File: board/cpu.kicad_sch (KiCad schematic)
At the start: 6 parts, among them U4 MC68000P

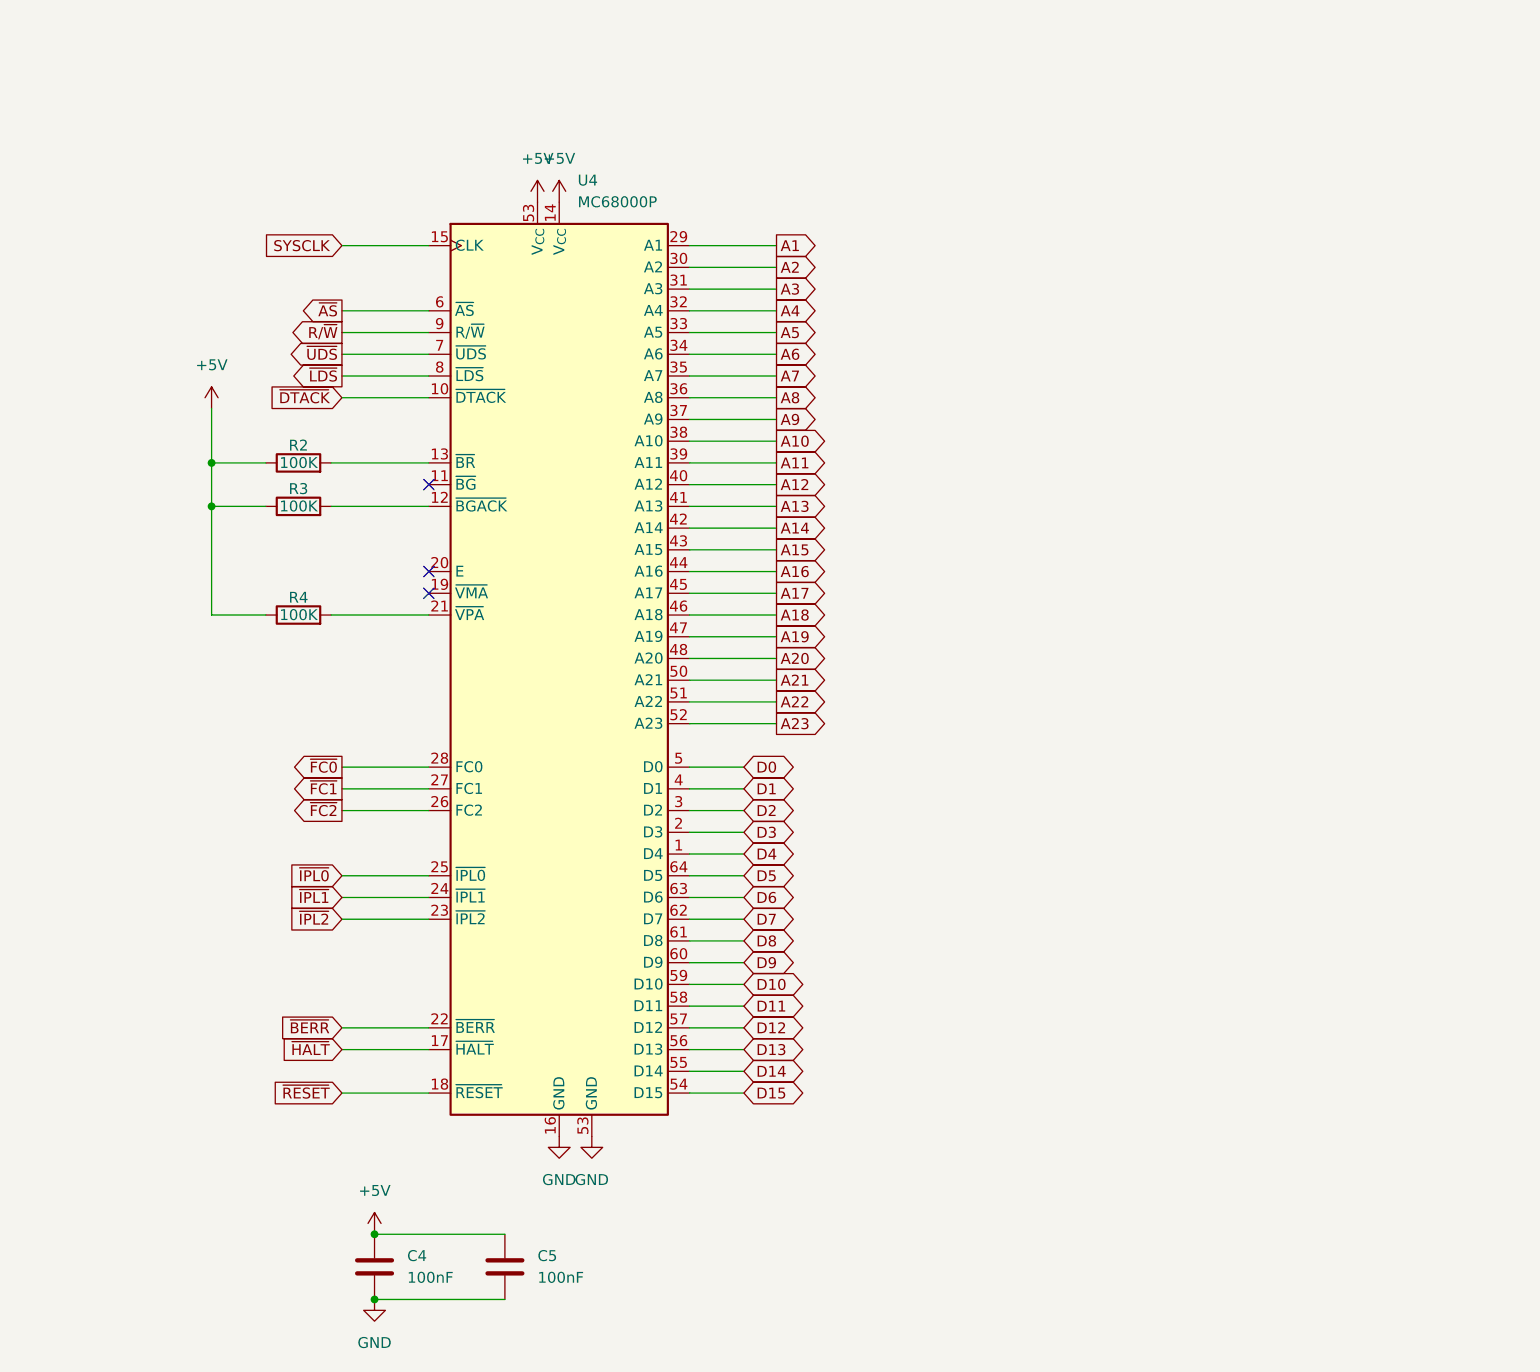
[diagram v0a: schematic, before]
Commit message: fill out most functionality - passes ERC
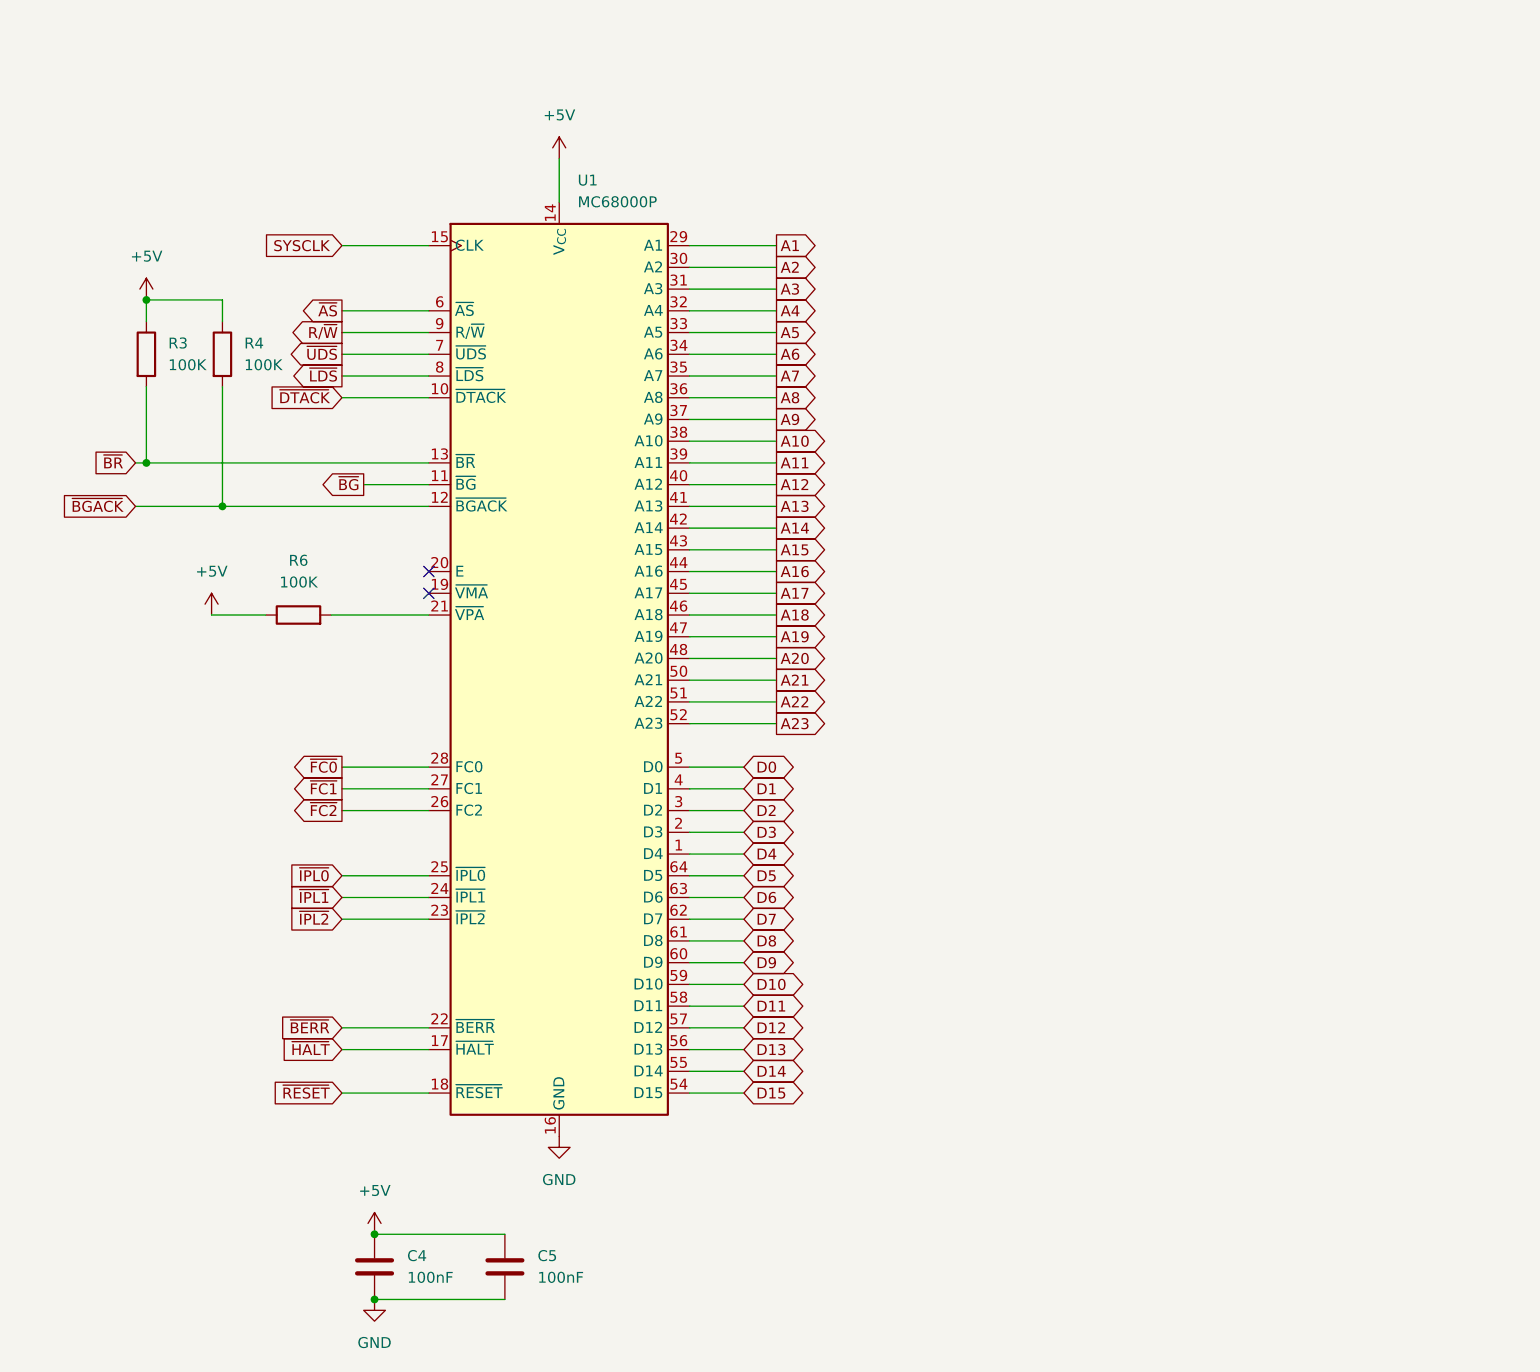
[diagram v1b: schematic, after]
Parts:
- removed R2, R3, R4: 100K, Resistors_SMD:R_0805, symbol MOBO_SMD-rescue:R
- added R3, R4, R6: 100K, symbol Device:R
- renumbered U4 to U1
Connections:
- net +5V: now also R3.1, R4.1, R6.1; no longer U1.53 (GND)
- net ~{BGACK}: now reaches U1.12 (~{BGACK})
- net ~{BGACK}: now also R4.2
- net ~{BG}: now reaches U1.11 (~{BG})
- net ~{BR}: now reaches U1.13 (~{BR})
- net ~{BR}: now also R3.2
- net at U1.21 (~{VPA}): now also R6.2
- no-connect marks 3 -> 2

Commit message: design draft complete, added footprints
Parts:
- added R13, R34, R54, R55: 10K, Resistor_THT:R_Axial_DIN0207_L6.3mm_D2.5mm_P10.16mm_Horizontal, symbol Device:R
- C4, C5: footprint (none) -> Capacitor_THT:C_Disc_D5.0mm_W2.5mm_P5.00mm
- R3, R4, R6: footprint (none) -> Resistor_THT:R_Axial_DIN0207_L6.3mm_D2.5mm_P10.16mm_Horizontal
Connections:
- net +5V: now also R13.1, R34.1, R54.1, R55.1
- net ~{HALT}: now also R54.2
- net ~{IPL0}: now also R13.2
- net ~{IPL1}: now also R34.2
- net ~{IPL2}: now also R55.2
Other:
- moved on the sheet: C4, C5, R3, R4, R6, U1

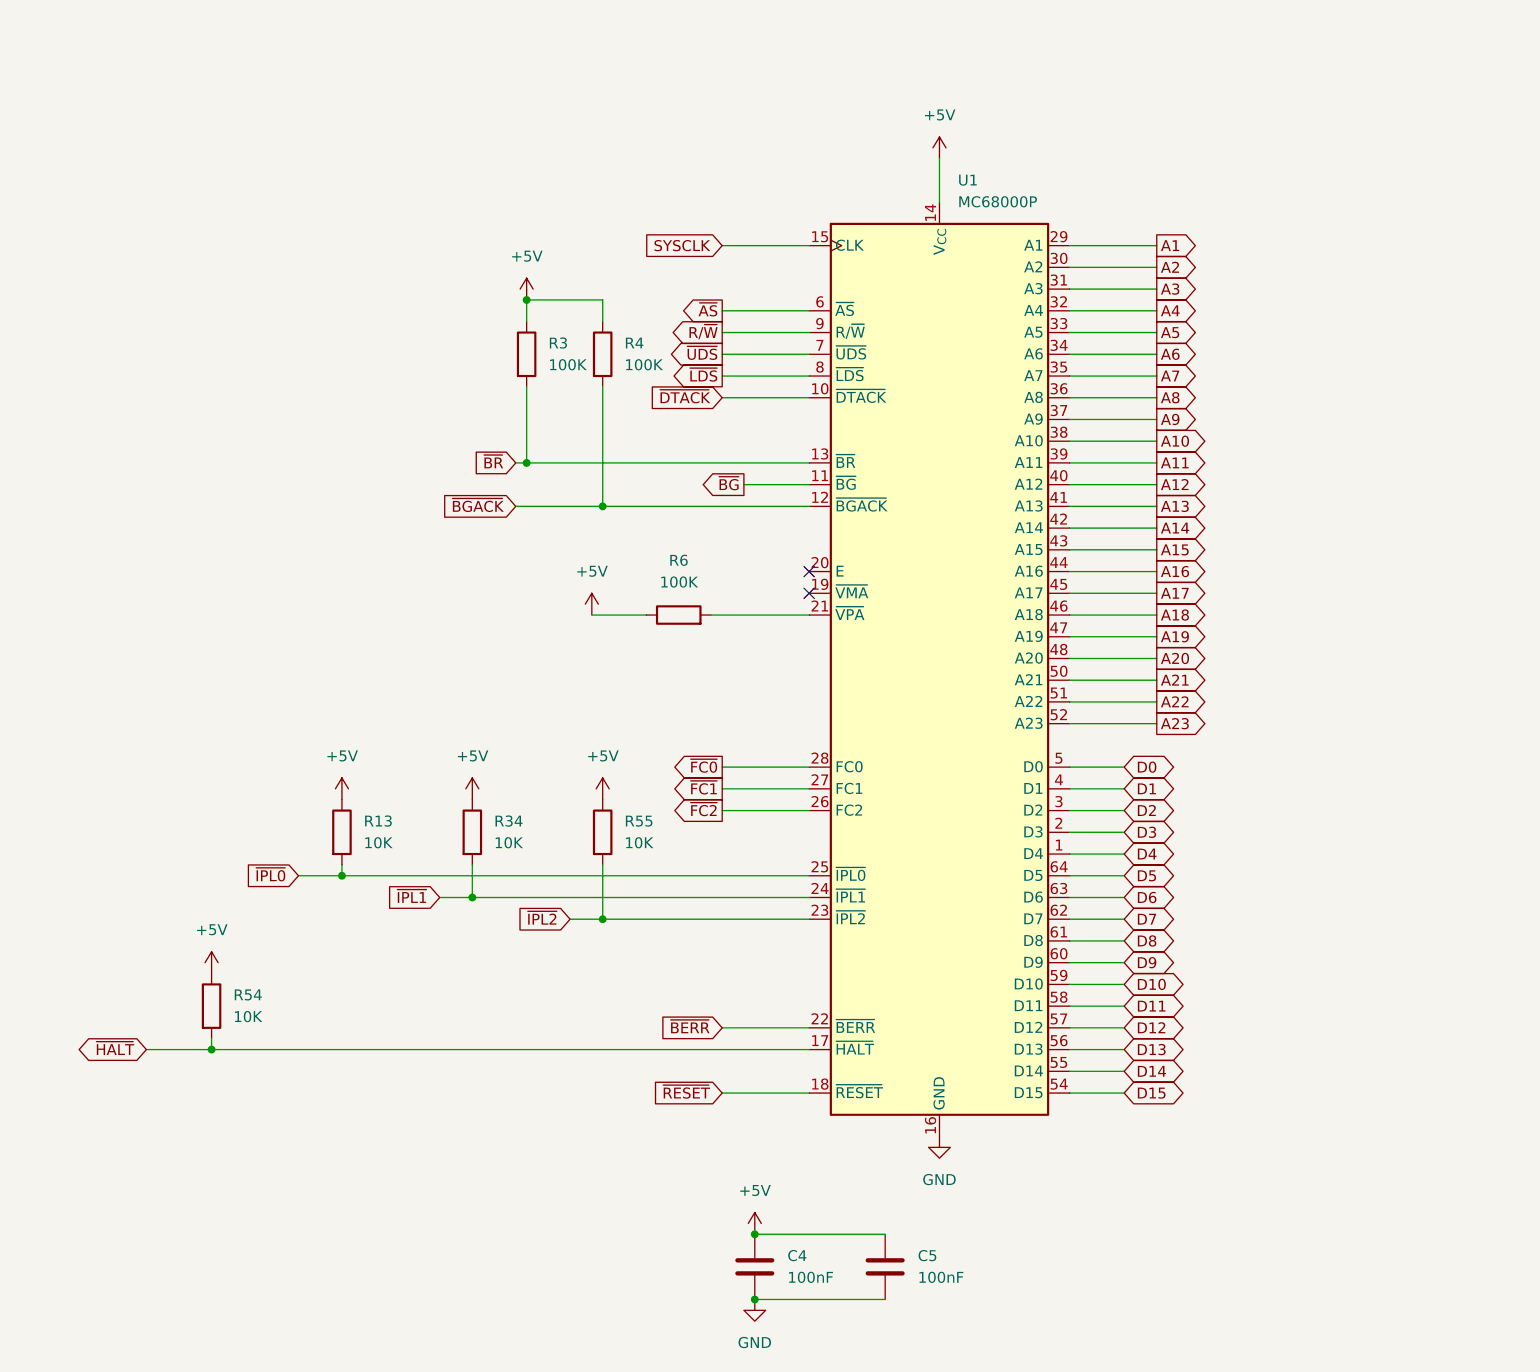
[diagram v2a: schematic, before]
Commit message: start of PCB and MMU
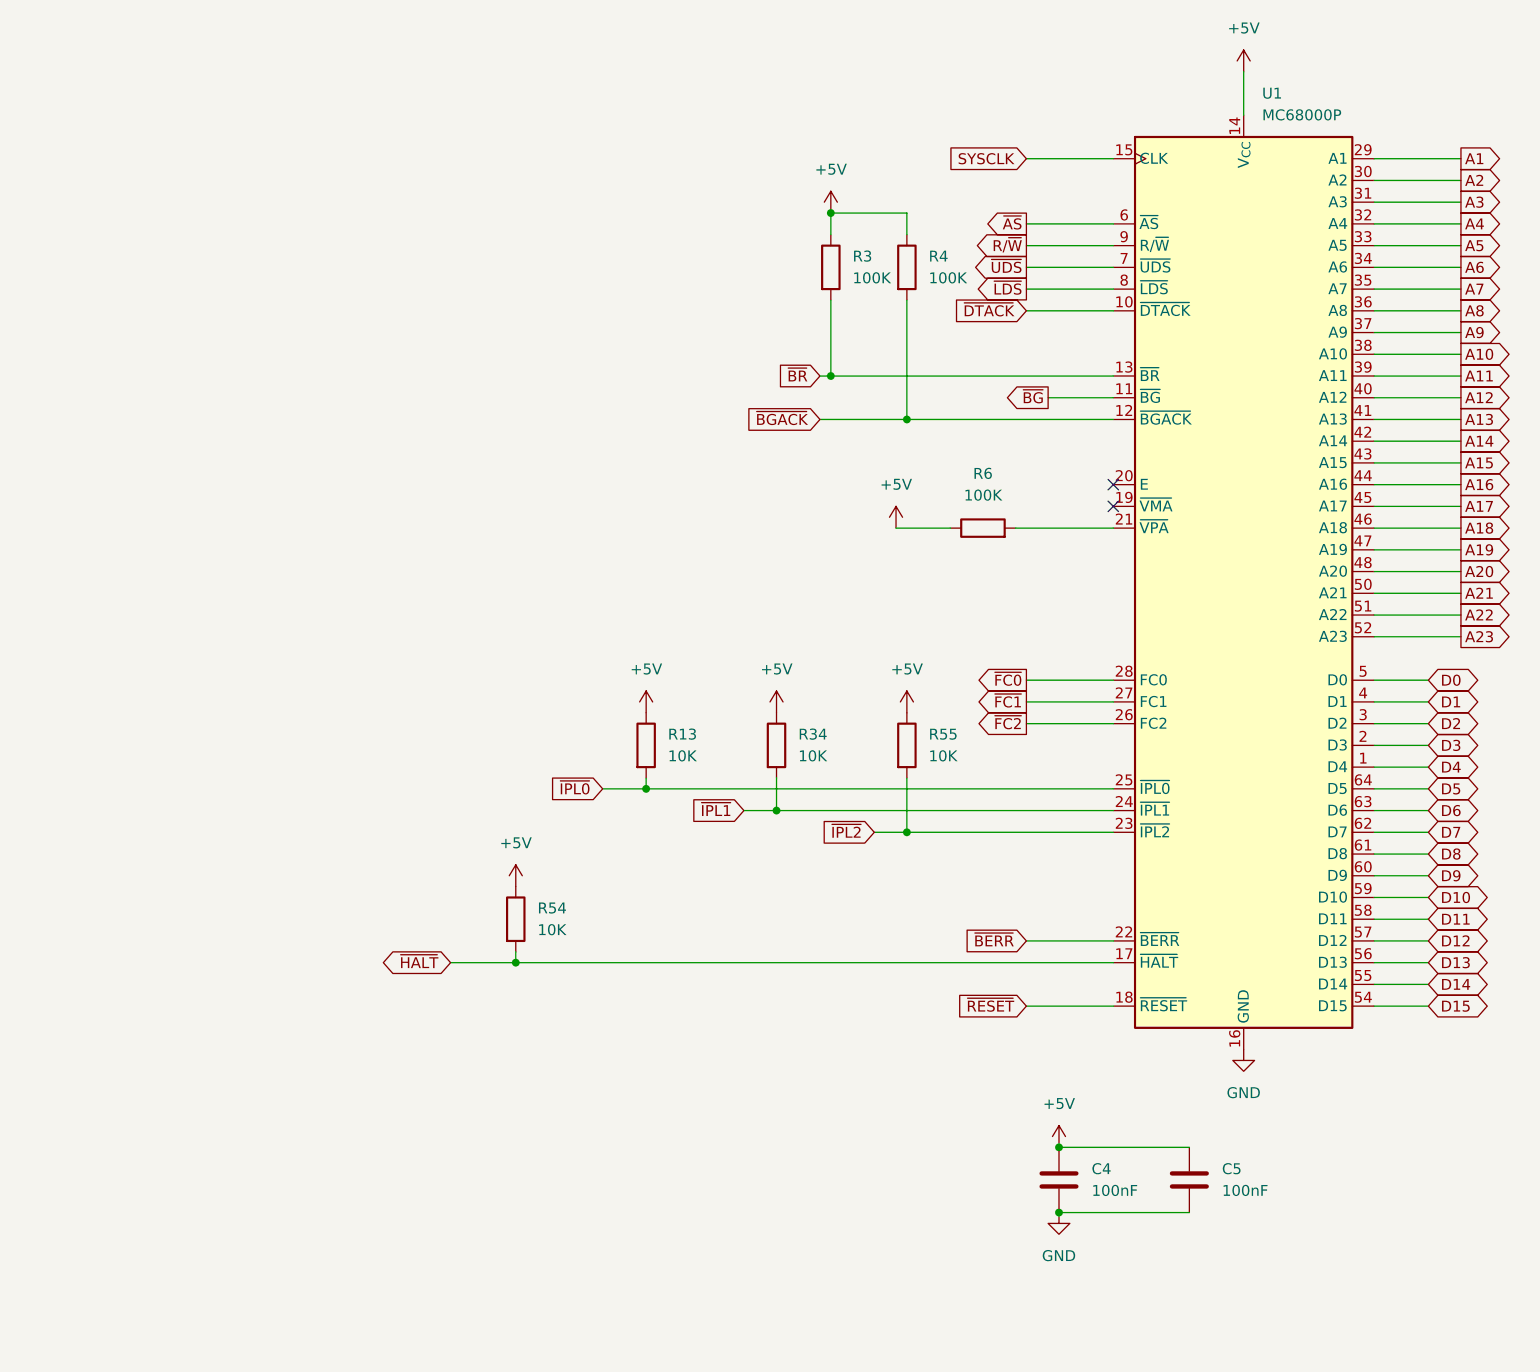
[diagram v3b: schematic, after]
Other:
- moved on the sheet: C4, C5, R13, R3, R34, R4, R54, R55, R6, U1

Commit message: checkpoint
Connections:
- net SYSCLK renamed CPUCLK
- net ~{FC0} renamed FC0
- net ~{FC1} renamed FC1
- net ~{FC2} renamed FC2
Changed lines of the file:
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@@
 		)
 	)
-	(global_label "~{FC1}"
+	(global_label "FC1"
 		(shape output)
 		(at 133.35 100.33 180)
@@
 		)
 	)
-	(global_label "SYSCLK"
+	(global_label "CPUCLK"
 		(shape input)
 		(at 133.35 36.83 180)
@@
 		)
 	)
-	(global_label "~{FC2}"
+	(global_label "FC2"
 		(shape output)
 		(at 133.35 102.87 180)
@@
 		)
 	)
-	(global_label "~{FC0}"
+	(global_label "FC0"
 		(shape output)
 		(at 133.35 97.79 180)

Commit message: Board rev1 PCB complete, already have a spot fix
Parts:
- removed R13, R34, R54, R55: 10K, Resistor_THT:R_Axial_DIN0207_L6.3mm_D2.5mm_P10.16mm_Horizontal, symbol Device:R
